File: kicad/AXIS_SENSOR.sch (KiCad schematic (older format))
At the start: 3 parts, among them U9 ICM-20602

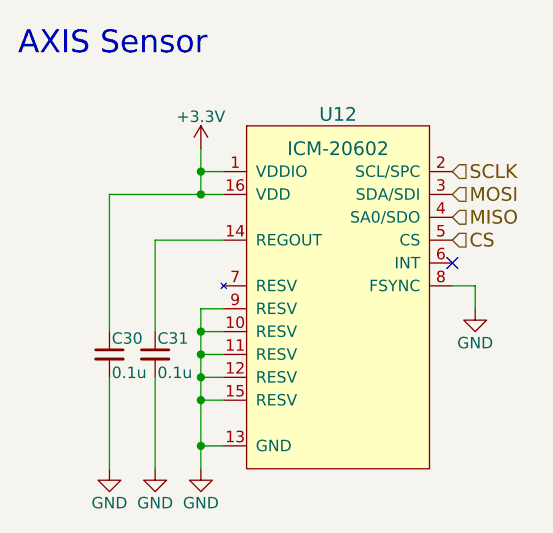
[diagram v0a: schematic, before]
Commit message: 回路を改良
受光部をフォトトランジスタに変更
測距センサをVL6180Xに変更
動作電圧を3Vに変更
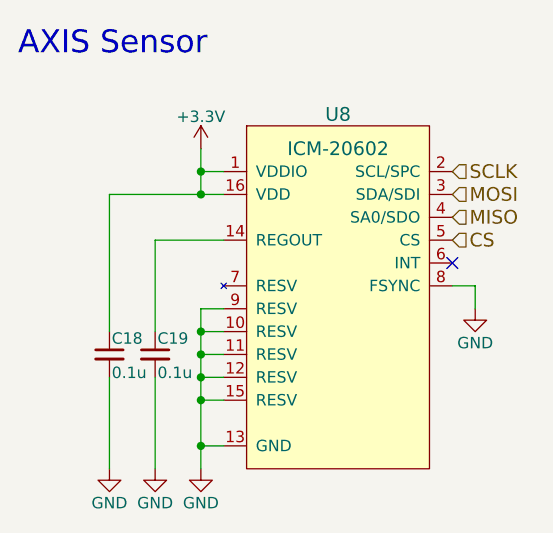
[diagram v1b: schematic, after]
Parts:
- U7: renamed from U9; footprint mouse:LGA-16-3x3 -> mouse:ICM-20602
- renumbered C20 to C14, C21 to C15
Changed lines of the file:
@@
 LIBS:ftdi
 LIBS:gennum
-LIBS:graphic
 LIBS:hc11
 LIBS:ir
 LIBS:Lattice
 LIBS:leds
-LIBS:logo
 LIBS:maxim
 LIBS:mechanical
@@
 LIBS:zetex
 LIBS:Zilog
+LIBS:graphic_symbols
+LIBS:infineon
+LIBS:intersil
+LIBS:LEM
+LIBS:logic_programmable
+LIBS:RFSolutions
 LIBS:KERISE-cache
 EELAYER 25 0
@@
 $Descr A4 11693 8268
 encoding utf-8
-Sheet 15 15
+Sheet 14 15
 Title ""
 Date ""
@@
 AXIS Sensor
 $Comp
-L ICM-20602 U9
+L ICM-20602 U7
 U 1 1 592C611A
 P 5600 3400
-AR Path="/57CC33F6/592C611A" Ref="U9"  Part="1"
-AR Path="/5A18D4D6/592C611A" Ref="U12"  Part="1"
-F 0 "U12" H 5600 4150 60  0000 C CNN
+AR Path="/57CC33F6/592C611A" Ref="U7"  Part="1"
+AR Path="/5A18D4D6/592C611A" Ref="U8"  Part="1"
+F 0 "U8" H 5600 4150 60  0000 C CNN
 F 1 "ICM-20602" H 5600 4000 60  0000 C CNN
-F 2 "mouse:LGA-16-3x3" H 5600 4000 60  0001 C CNN
+F 2 "mouse:ICM-20602" H 5600 4000 60  0001 C CNN
 F 3 "" H 5600 4000 60  0000 C CNN
 	1    5600 3400
@@
 $EndComp
 $Comp
-L C_Small C21
+L C_Small C15
 U 1 1 592C613A
 P 4800 3700
-AR Path="/57CC33F6/592C613A" Ref="C21"  Part="1"
-AR Path="/5A18D4D6/592C613A" Ref="C31"  Part="1"
-F 0 "C31" H 4810 3770 50  0000 L CNN
+AR Path="/57CC33F6/592C613A" Ref="C15"  Part="1"
+AR Path="/5A18D4D6/592C613A" Ref="C19"  Part="1"
+F 0 "C19" H 4810 3770 50  0000 L CNN
 F 1 "0.1u" H 4810 3620 50  0000 L CNN
 F 2 "Capacitors_SMD:C_0201" H 4800 3700 50  0001 C CNN
@@
 $EndComp
 $Comp
-L C_Small C20
+L C_Small C14
 U 1 1 592C6186
 P 4600 3700
-AR Path="/57CC33F6/592C6186" Ref="C20"  Part="1"
-AR Path="/5A18D4D6/592C6186" Ref="C30"  Part="1"
-F 0 "C30" H 4610 3770 50  0000 L CNN
+AR Path="/57CC33F6/592C6186" Ref="C14"  Part="1"
+AR Path="/5A18D4D6/592C6186" Ref="C18"  Part="1"
+F 0 "C18" H 4610 3770 50  0000 L CNN
 F 1 "0.1u" H 4610 3620 50  0000 L CNN
 F 2 "Capacitors_SMD:C_0201" H 4600 3700 50  0001 C CNN
@@
 $EndComp
 $Comp
-L GND #PWR062
+L GND #PWR060
 U 1 1 592C63E1
 P 5000 4200
-AR Path="/57CC33F6/592C63E1" Ref="#PWR062"  Part="1"
-AR Path="/5A18D4D6/592C63E1" Ref="#PWR077"  Part="1"
-F 0 "#PWR077" H 5000 3950 50  0001 C CNN
+AR Path="/57CC33F6/592C63E1" Ref="#PWR060"  Part="1"
+AR Path="/5A18D4D6/592C63E1" Ref="#PWR071"  Part="1"
+F 0 "#PWR071" H 5000 3950 50  0001 C CNN
 F 1 "GND" H 5000 4050 50  0000 C CNN
 F 2 "" H 5000 4200 50  0000 C CNN
@@
 $EndComp
 $Comp
-L GND #PWR063
+L GND #PWR061
 U 1 1 592C640D
 P 4800 4200
-AR Path="/57CC33F6/592C640D" Ref="#PWR063"  Part="1"
-AR Path="/5A18D4D6/592C640D" Ref="#PWR078"  Part="1"
-F 0 "#PWR078" H 4800 3950 50  0001 C CNN
+AR Path="/57CC33F6/592C640D" Ref="#PWR061"  Part="1"
+AR Path="/5A18D4D6/592C640D" Ref="#PWR072"  Part="1"
+F 0 "#PWR072" H 4800 3950 50  0001 C CNN
 F 1 "GND" H 4800 4050 50  0000 C CNN
 F 2 "" H 4800 4200 50  0000 C CNN
@@
 $EndComp
 $Comp
-L GND #PWR064
+L GND #PWR062
 U 1 1 592C6444
 P 4600 4200
-AR Path="/57CC33F6/592C6444" Ref="#PWR064"  Part="1"
-AR Path="/5A18D4D6/592C6444" Ref="#PWR079"  Part="1"
-F 0 "#PWR079" H 4600 3950 50  0001 C CNN
+AR Path="/57CC33F6/592C6444" Ref="#PWR062"  Part="1"
+AR Path="/5A18D4D6/592C6444" Ref="#PWR073"  Part="1"
+F 0 "#PWR073" H 4600 3950 50  0001 C CNN
 F 1 "GND" H 4600 4050 50  0000 C CNN
 F 2 "" H 4600 4200 50  0000 C CNN
@@
 $EndComp
 $Comp
-L +3.3V #PWR065
+L +3.3V #PWR063
 U 1 1 592C64FB
 P 5000 2800
-AR Path="/57CC33F6/592C64FB" Ref="#PWR065"  Part="1"
-AR Path="/5A18D4D6/592C64FB" Ref="#PWR080"  Part="1"
-F 0 "#PWR080" H 5000 2650 50  0001 C CNN
+AR Path="/57CC33F6/592C64FB" Ref="#PWR063"  Part="1"
+AR Path="/5A18D4D6/592C64FB" Ref="#PWR074"  Part="1"
+F 0 "#PWR074" H 5000 2650 50  0001 C CNN
 F 1 "+3.3V" H 5000 2940 50  0000 C CNN
 F 2 "" H 5000 2800 50  0000 C CNN
@@
 NoConn ~ 6100 3300
 $Comp
-L GND #PWR066
+L GND #PWR064
 U 1 1 592C6B85
 P 6200 3500
-AR Path="/57CC33F6/592C6B85" Ref="#PWR066"  Part="1"
-AR Path="/5A18D4D6/592C6B85" Ref="#PWR081"  Part="1"
-F 0 "#PWR081" H 6200 3250 50  0001 C CNN
+AR Path="/57CC33F6/592C6B85" Ref="#PWR064"  Part="1"
+AR Path="/5A18D4D6/592C6B85" Ref="#PWR075"  Part="1"
+F 0 "#PWR075" H 6200 3250 50  0001 C CNN
 F 1 "GND" H 6200 3350 50  0000 C CNN
 F 2 "" H 6200 3500 50  0000 C CNN

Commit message: 部品を配置
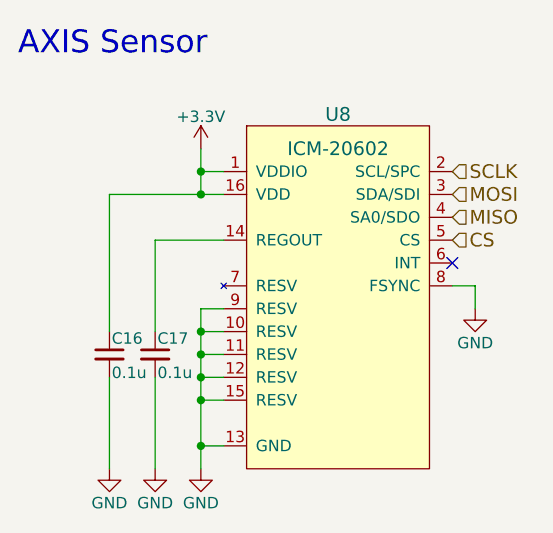
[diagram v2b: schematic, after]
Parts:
- C12: renamed from C14; footprint Capacitors_SMD:C_0201 -> Capacitors_SMD:C_0201_NoSilk
- C13: renamed from C15; footprint Capacitors_SMD:C_0201 -> Capacitors_SMD:C_0201_NoSilk
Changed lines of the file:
@@
 $Descr A4 11693 8268
 encoding utf-8
-Sheet 14 15
+Sheet 14 16
 Title ""
 Date ""
@@
 $EndComp
 $Comp
-L C_Small C15
+L C_Small C13
 U 1 1 592C613A
 P 4800 3700
-AR Path="/57CC33F6/592C613A" Ref="C15"  Part="1"
-AR Path="/5A18D4D6/592C613A" Ref="C19"  Part="1"
-F 0 "C19" H 4810 3770 50  0000 L CNN
+AR Path="/57CC33F6/592C613A" Ref="C13"  Part="1"
+AR Path="/5A18D4D6/592C613A" Ref="C17"  Part="1"
+F 0 "C17" H 4810 3770 50  0000 L CNN
 F 1 "0.1u" H 4810 3620 50  0000 L CNN
-F 2 "Capacitors_SMD:C_0201" H 4800 3700 50  0001 C CNN
+F 2 "Capacitors_SMD:C_0201_NoSilk" H 4800 3700 50  0001 C CNN
 F 3 "" H 4800 3700 50  0000 C CNN
 	1    4800 3700
@@
 $EndComp
 $Comp
-L C_Small C14
+L C_Small C12
 U 1 1 592C6186
 P 4600 3700
-AR Path="/57CC33F6/592C6186" Ref="C14"  Part="1"
-AR Path="/5A18D4D6/592C6186" Ref="C18"  Part="1"
-F 0 "C18" H 4610 3770 50  0000 L CNN
+AR Path="/57CC33F6/592C6186" Ref="C12"  Part="1"
+AR Path="/5A18D4D6/592C6186" Ref="C16"  Part="1"
+F 0 "C16" H 4610 3770 50  0000 L CNN
 F 1 "0.1u" H 4610 3620 50  0000 L CNN
-F 2 "Capacitors_SMD:C_0201" H 4600 3700 50  0001 C CNN
+F 2 "Capacitors_SMD:C_0201_NoSilk" H 4600 3700 50  0001 C CNN
 F 3 "" H 4600 3700 50  0000 C CNN
 	1    4600 3700
@@
 $EndComp
 $Comp
-L GND #PWR060
+L GND #PWR058
 U 1 1 592C63E1
 P 5000 4200
-AR Path="/57CC33F6/592C63E1" Ref="#PWR060"  Part="1"
-AR Path="/5A18D4D6/592C63E1" Ref="#PWR071"  Part="1"
-F 0 "#PWR071" H 5000 3950 50  0001 C CNN
+AR Path="/57CC33F6/592C63E1" Ref="#PWR058"  Part="1"
+AR Path="/5A18D4D6/592C63E1" Ref="#PWR069"  Part="1"
+F 0 "#PWR069" H 5000 3950 50  0001 C CNN
 F 1 "GND" H 5000 4050 50  0000 C CNN
 F 2 "" H 5000 4200 50  0000 C CNN
@@
 $EndComp
 $Comp
-L GND #PWR061
+L GND #PWR059
 U 1 1 592C640D
 P 4800 4200
-AR Path="/57CC33F6/592C640D" Ref="#PWR061"  Part="1"
-AR Path="/5A18D4D6/592C640D" Ref="#PWR072"  Part="1"
-F 0 "#PWR072" H 4800 3950 50  0001 C CNN
+AR Path="/57CC33F6/592C640D" Ref="#PWR059"  Part="1"
+AR Path="/5A18D4D6/592C640D" Ref="#PWR070"  Part="1"
+F 0 "#PWR070" H 4800 3950 50  0001 C CNN
 F 1 "GND" H 4800 4050 50  0000 C CNN
 F 2 "" H 4800 4200 50  0000 C CNN
@@
 $EndComp
 $Comp
-L GND #PWR062
+L GND #PWR060
 U 1 1 592C6444
 P 4600 4200
-AR Path="/57CC33F6/592C6444" Ref="#PWR062"  Part="1"
-AR Path="/5A18D4D6/592C6444" Ref="#PWR073"  Part="1"
-F 0 "#PWR073" H 4600 3950 50  0001 C CNN
+AR Path="/57CC33F6/592C6444" Ref="#PWR060"  Part="1"
+AR Path="/5A18D4D6/592C6444" Ref="#PWR071"  Part="1"
+F 0 "#PWR071" H 4600 3950 50  0001 C CNN
 F 1 "GND" H 4600 4050 50  0000 C CNN
 F 2 "" H 4600 4200 50  0000 C CNN
@@
 $EndComp
 $Comp
-L +3.3V #PWR063
+L +3.3V #PWR061
 U 1 1 592C64FB
 P 5000 2800
-AR Path="/57CC33F6/592C64FB" Ref="#PWR063"  Part="1"
-AR Path="/5A18D4D6/592C64FB" Ref="#PWR074"  Part="1"
-F 0 "#PWR074" H 5000 2650 50  0001 C CNN
+AR Path="/57CC33F6/592C64FB" Ref="#PWR061"  Part="1"
+AR Path="/5A18D4D6/592C64FB" Ref="#PWR072"  Part="1"
+F 0 "#PWR072" H 5000 2650 50  0001 C CNN
 F 1 "+3.3V" H 5000 2940 50  0000 C CNN
 F 2 "" H 5000 2800 50  0000 C CNN
@@
 NoConn ~ 6100 3300
 $Comp
-L GND #PWR064
+L GND #PWR062
 U 1 1 592C6B85
 P 6200 3500
-AR Path="/57CC33F6/592C6B85" Ref="#PWR064"  Part="1"
-AR Path="/5A18D4D6/592C6B85" Ref="#PWR075"  Part="1"
-F 0 "#PWR075" H 6200 3250 50  0001 C CNN
+AR Path="/57CC33F6/592C6B85" Ref="#PWR062"  Part="1"
+AR Path="/5A18D4D6/592C6B85" Ref="#PWR073"  Part="1"
+F 0 "#PWR073" H 6200 3250 50  0001 C CNN
 F 1 "GND" H 6200 3350 50  0000 C CNN
 F 2 "" H 6200 3500 50  0000 C CNN

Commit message: 回路を編集 ToFを除去
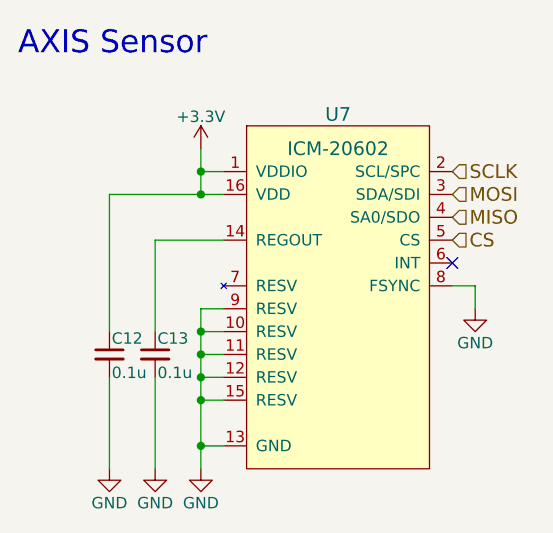
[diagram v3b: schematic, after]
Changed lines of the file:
@@
 $Descr A4 11693 8268
 encoding utf-8
-Sheet 14 16
+Sheet 11 15
 Title ""
 Date ""
@@
 AR Path="/57CC33F6/592C611A" Ref="U7"  Part="1"
 AR Path="/5A18D4D6/592C611A" Ref="U8"  Part="1"
-F 0 "U8" H 5600 4150 60  0000 C CNN
+F 0 "U7" H 5600 4150 60  0000 C CNN
 F 1 "ICM-20602" H 5600 4000 60  0000 C CNN
 F 2 "mouse:ICM-20602" H 5600 4000 60  0001 C CNN
@@
 AR Path="/57CC33F6/592C613A" Ref="C13"  Part="1"
 AR Path="/5A18D4D6/592C613A" Ref="C17"  Part="1"
-F 0 "C17" H 4810 3770 50  0000 L CNN
+F 0 "C13" H 4810 3770 50  0000 L CNN
 F 1 "0.1u" H 4810 3620 50  0000 L CNN
 F 2 "Capacitors_SMD:C_0201_NoSilk" H 4800 3700 50  0001 C CNN
@@
 AR Path="/57CC33F6/592C6186" Ref="C12"  Part="1"
 AR Path="/5A18D4D6/592C6186" Ref="C16"  Part="1"
-F 0 "C16" H 4610 3770 50  0000 L CNN
+F 0 "C12" H 4610 3770 50  0000 L CNN
 F 1 "0.1u" H 4610 3620 50  0000 L CNN
 F 2 "Capacitors_SMD:C_0201_NoSilk" H 4600 3700 50  0001 C CNN

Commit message: 部品を配置 kicad5
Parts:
- C10: renamed from C12; symbol C_Small -> Device:C_Small
- C11: renamed from C13; symbol C_Small -> Device:C_Small
- U6: renamed from U7; symbol ICM-20602 -> KERISE:ICM-20602
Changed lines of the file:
@@
-EESchema Schematic File Version 2
-LIBS:power
-LIBS:device
-LIBS:transistors
-LIBS:conn
-LIBS:linear
-LIBS:regul
-LIBS:74xx
-LIBS:cmos4000
-LIBS:adc-dac
-LIBS:memory
-LIBS:xilinx
-LIBS:microcontrollers
-LIBS:dsp
-LIBS:microchip
-LIBS:analog_switches
-LIBS:motorola
-LIBS:texas
-LIBS:intel
-LIBS:audio
-LIBS:interface
-LIBS:digital-audio
-LIBS:philips
-LIBS:display
-LIBS:cypress
-LIBS:siliconi
-LIBS:opto
-LIBS:atmel
-LIBS:contrib
-LIBS:valves
-LIBS:KERISE
-LIBS:74xgxx
-LIBS:ac-dc
-LIBS:actel
-LIBS:allegro
-LIBS:Altera
-LIBS:analog_devices
-LIBS:battery_management
-LIBS:bbd
-LIBS:bosch
-LIBS:brooktre
-LIBS:cmos_ieee
-LIBS:dc-dc
-LIBS:diode
-LIBS:elec-unifil
-LIBS:ESD_Protection
-LIBS:ftdi
-LIBS:gennum
-LIBS:hc11
-LIBS:ir
-LIBS:Lattice
-LIBS:leds
-LIBS:maxim
-LIBS:mechanical
-LIBS:microchip_dspic33dsc
-LIBS:microchip_pic10mcu
-LIBS:microchip_pic12mcu
-LIBS:microchip_pic16mcu
-LIBS:microchip_pic18mcu
-LIBS:microchip_pic24mcu
-LIBS:microchip_pic32mcu
-LIBS:modules
-LIBS:motor_drivers
-LIBS:motors
-LIBS:msp430
-LIBS:nordicsemi
-LIBS:nxp
-LIBS:nxp_armmcu
-LIBS:onsemi
-LIBS:Oscillators
-LIBS:Power_Management
-LIBS:powerint
-LIBS:pspice
-LIBS:references
-LIBS:relays
-LIBS:rfcom
-LIBS:sensors
-LIBS:silabs
-LIBS:stm8
-LIBS:stm32
-LIBS:supertex
-LIBS:switches
-LIBS:transf
-LIBS:triac_thyristor
-LIBS:ttl_ieee
-LIBS:video
-LIBS:wiznet
-LIBS:Worldsemi
-LIBS:Xicor
-LIBS:zetex
-LIBS:Zilog
-LIBS:graphic_symbols
-LIBS:infineon
-LIBS:intersil
-LIBS:LEM
-LIBS:logic_programmable
-LIBS:RFSolutions
+EESchema Schematic File Version 4
 LIBS:KERISE-cache
-EELAYER 25 0
+EELAYER 26 0
 EELAYER END
 $Descr A4 11693 8268
 encoding utf-8
-Sheet 11 15
+Sheet 10 14
 Title ""
 Date ""
@@
 AXIS Sensor
 $Comp
-L ICM-20602 U7
+L KERISE:ICM-20602 U6
 U 1 1 592C611A
 P 5600 3400
-AR Path="/57CC33F6/592C611A" Ref="U7"  Part="1"
-AR Path="/5A18D4D6/592C611A" Ref="U8"  Part="1"
+AR Path="/57CC33F6/592C611A" Ref="U6"  Part="1"
+AR Path="/5A18D4D6/592C611A" Ref="U7"  Part="1"
 F 0 "U7" H 5600 4150 60  0000 C CNN
 F 1 "ICM-20602" H 5600 4000 60  0000 C CNN
@@
 $EndComp
 $Comp
-L C_Small C13
+L Device:C_Small C11
 U 1 1 592C613A
 P 4800 3700
-AR Path="/57CC33F6/592C613A" Ref="C13"  Part="1"
-AR Path="/5A18D4D6/592C613A" Ref="C17"  Part="1"
-F 0 "C13" H 4810 3770 50  0000 L CNN
+AR Path="/57CC33F6/592C613A" Ref="C11"  Part="1"
+AR Path="/5A18D4D6/592C613A" Ref="C15"  Part="1"
+F 0 "C15" H 4810 3770 50  0000 L CNN
 F 1 "0.1u" H 4810 3620 50  0000 L CNN
 F 2 "Capacitors_SMD:C_0201_NoSilk" H 4800 3700 50  0001 C CNN
@@
 $EndComp
 $Comp
-L C_Small C12
+L Device:C_Small C10
 U 1 1 592C6186
 P 4600 3700
-AR Path="/57CC33F6/592C6186" Ref="C12"  Part="1"
-AR Path="/5A18D4D6/592C6186" Ref="C16"  Part="1"
-F 0 "C12" H 4610 3770 50  0000 L CNN
+AR Path="/57CC33F6/592C6186" Ref="C10"  Part="1"
+AR Path="/5A18D4D6/592C6186" Ref="C14"  Part="1"
+F 0 "C14" H 4610 3770 50  0000 L CNN
 F 1 "0.1u" H 4610 3620 50  0000 L CNN
 F 2 "Capacitors_SMD:C_0201_NoSilk" H 4600 3700 50  0001 C CNN
@@
 $EndComp
 $Comp
-L GND #PWR058
+L power:GND #PWR050
 U 1 1 592C63E1
 P 5000 4200
-AR Path="/57CC33F6/592C63E1" Ref="#PWR058"  Part="1"
-AR Path="/5A18D4D6/592C63E1" Ref="#PWR069"  Part="1"
-F 0 "#PWR069" H 5000 3950 50  0001 C CNN
+AR Path="/57CC33F6/592C63E1" Ref="#PWR050"  Part="1"
+AR Path="/5A18D4D6/592C63E1" Ref="#PWR061"  Part="1"
+F 0 "#PWR061" H 5000 3950 50  0001 C CNN
 F 1 "GND" H 5000 4050 50  0000 C CNN
 F 2 "" H 5000 4200 50  0000 C CNN
@@
 $EndComp
 $Comp
-L GND #PWR059
+L power:GND #PWR048
 U 1 1 592C640D
 P 4800 4200
-AR Path="/57CC33F6/592C640D" Ref="#PWR059"  Part="1"
-AR Path="/5A18D4D6/592C640D" Ref="#PWR070"  Part="1"
-F 0 "#PWR070" H 4800 3950 50  0001 C CNN
+AR Path="/57CC33F6/592C640D" Ref="#PWR048"  Part="1"
+AR Path="/5A18D4D6/592C640D" Ref="#PWR059"  Part="1"
+F 0 "#PWR059" H 4800 3950 50  0001 C CNN
 F 1 "GND" H 4800 4050 50  0000 C CNN
 F 2 "" H 4800 4200 50  0000 C CNN
@@
 $EndComp
 $Comp
-L GND #PWR060
+L power:GND #PWR047
 U 1 1 592C6444
 P 4600 4200
-AR Path="/57CC33F6/592C6444" Ref="#PWR060"  Part="1"
-AR Path="/5A18D4D6/592C6444" Ref="#PWR071"  Part="1"
-F 0 "#PWR071" H 4600 3950 50  0001 C CNN
+AR Path="/57CC33F6/592C6444" Ref="#PWR047"  Part="1"
+AR Path="/5A18D4D6/592C6444" Ref="#PWR058"  Part="1"
+F 0 "#PWR058" H 4600 3950 50  0001 C CNN
 F 1 "GND" H 4600 4050 50  0000 C CNN
 F 2 "" H 4600 4200 50  0000 C CNN
@@
 $EndComp
 $Comp
-L +3.3V #PWR061
+L power:+3.3V #PWR049
 U 1 1 592C64FB
 P 5000 2800
-AR Path="/57CC33F6/592C64FB" Ref="#PWR061"  Part="1"
-AR Path="/5A18D4D6/592C64FB" Ref="#PWR072"  Part="1"
-F 0 "#PWR072" H 5000 2650 50  0001 C CNN
+AR Path="/57CC33F6/592C64FB" Ref="#PWR049"  Part="1"
+AR Path="/5A18D4D6/592C64FB" Ref="#PWR060"  Part="1"
+F 0 "#PWR060" H 5000 2650 50  0001 C CNN
 F 1 "+3.3V" H 5000 2940 50  0000 C CNN
 F 2 "" H 5000 2800 50  0000 C CNN
@@
 NoConn ~ 6100 3300
 $Comp
-L GND #PWR062
+L power:GND #PWR051
 U 1 1 592C6B85
 P 6200 3500
-AR Path="/57CC33F6/592C6B85" Ref="#PWR062"  Part="1"
-AR Path="/5A18D4D6/592C6B85" Ref="#PWR073"  Part="1"
-F 0 "#PWR073" H 6200 3250 50  0001 C CNN
+AR Path="/57CC33F6/592C6B85" Ref="#PWR051"  Part="1"
+AR Path="/5A18D4D6/592C6B85" Ref="#PWR062"  Part="1"
+F 0 "#PWR062" H 6200 3250 50  0001 C CNN
 F 1 "GND" H 6200 3350 50  0000 C CNN
 F 2 "" H 6200 3500 50  0000 C CNN
@@
 SCLK
 Wire Wire Line
-	4600 3000 5100 3000
+	4600 3000 5000 3000
 Wire Wire Line
 	4600 4200 4600 3800
@@
 	5000 3900 5100 3900
 Wire Wire Line
-	5000 3500 5000 4200
+	5000 3500 5000 3600
 Wire Wire Line
 	5000 4100 5100 4100
@@
 Connection ~ 5000 3000
 Wire Wire Line
-	5000 2800 5000 3000
+	5000 2800 5000 2900
+Wire Wire Line
+	5000 4100 5000 4200
+Wire Wire Line
+	5000 3600 5000 3700
+Wire Wire Line
+	5000 3700 5000 3800
+Wire Wire Line
+	5000 3800 5000 3900
+Wire Wire Line
+	5000 3900 5000 4100
+Wire Wire Line
+	5000 2900 5000 3000
+Wire Wire Line
+	5000 3000 5100 3000
 $EndSCHEMATC
